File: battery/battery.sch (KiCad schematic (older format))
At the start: 40 parts, among them J1 batt_1, J2 batt_2, J3 batt_3, J4 batt_4, J5 reed_switch, J6 toPcb+, J7 toPcb-, J8 on_signal, Q1 batt1_sw, Q2 batt2_sw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

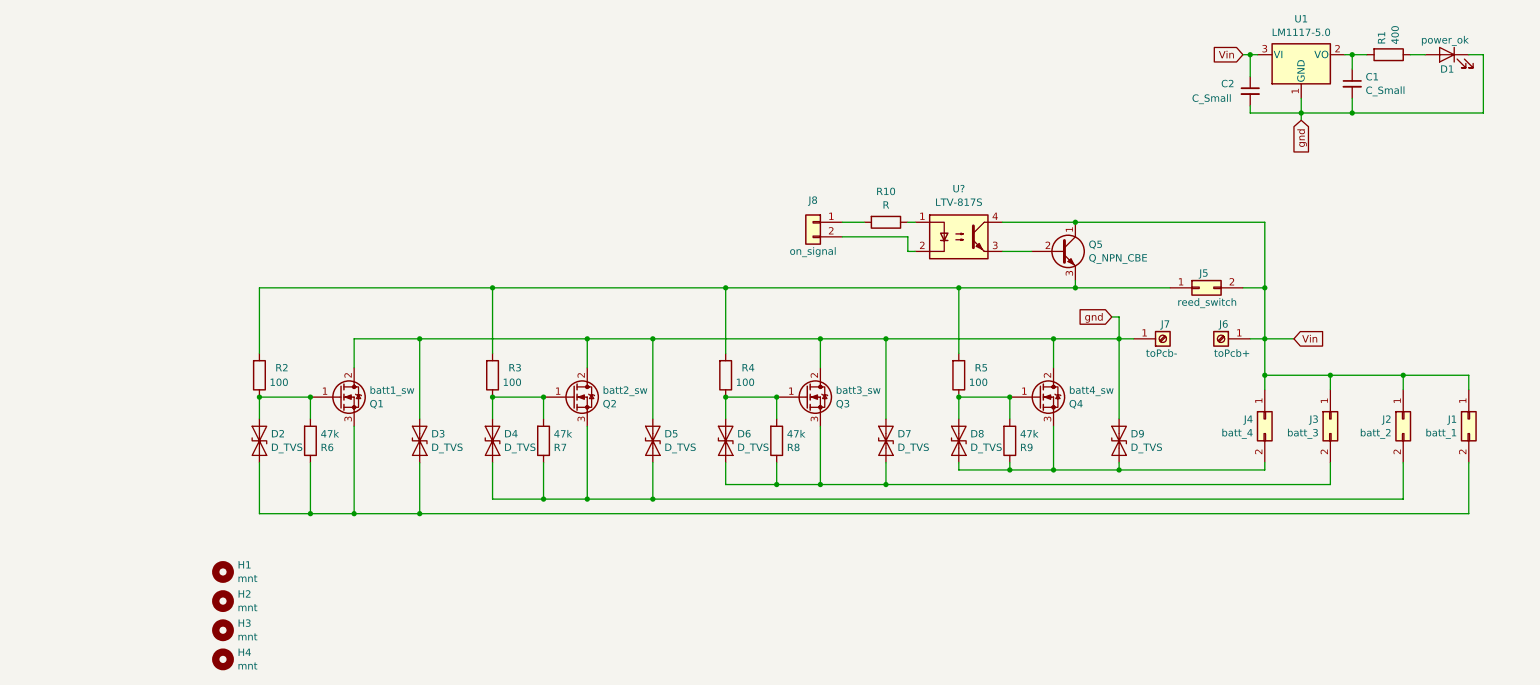
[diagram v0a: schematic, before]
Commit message: capacitor bybpas
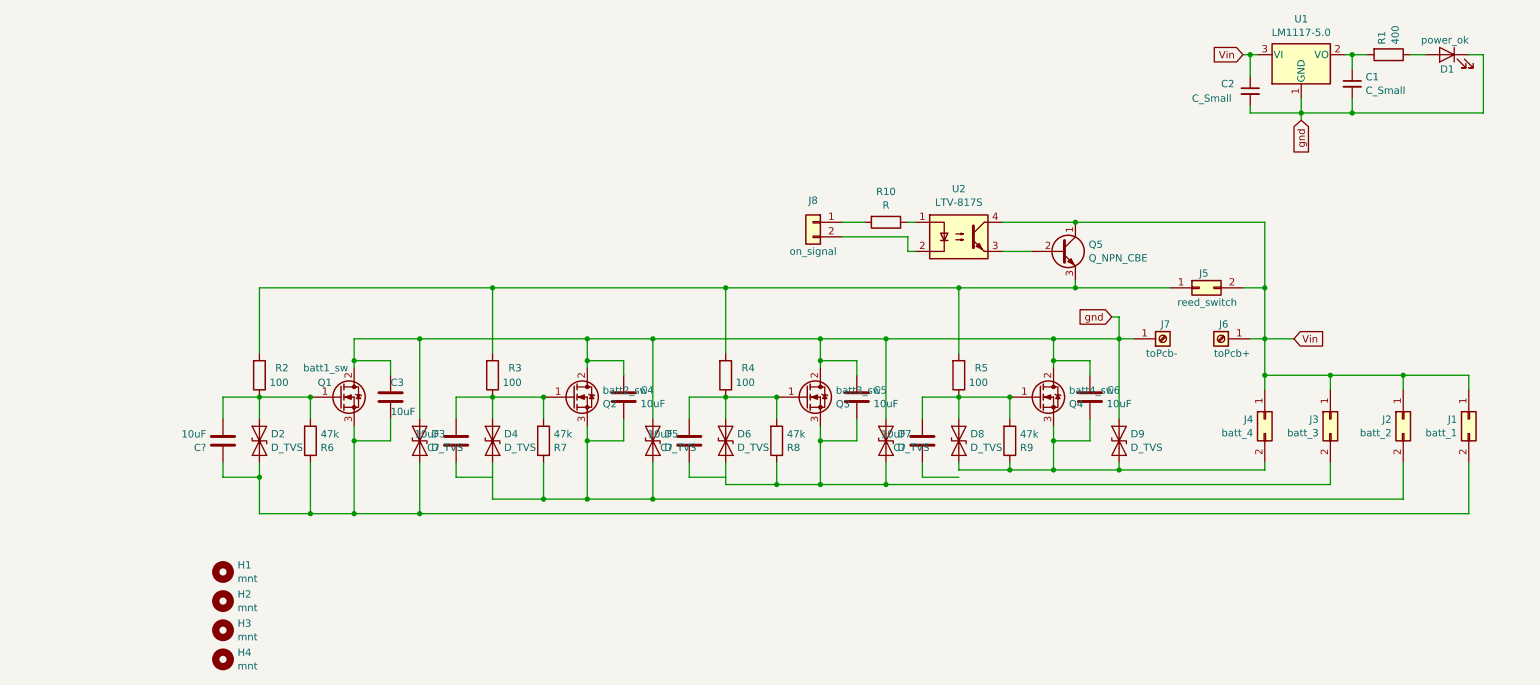
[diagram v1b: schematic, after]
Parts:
- added C3, C4, C5, C6, C? (x4): 10uF, Capacitor_SMD:C_0805_2012Metric_Pad1.15x1.40mm_HandSolder, symbol Device:C
- D2, D3, D4, D5, D6, D7, D8, D9: footprint Diode_SMD:D_SMB_Handsoldering -> Diode_SMD:D_SMB
- Q5: footprint Package_TO_SOT_THT:TO-92 -> Package_TO_SOT_SMD:SOT-23
- gave numbers to parts that had none: 1
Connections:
- net gnd: now also C3.1, C4.1, C5.1, C6.1
- net at D2.1 (A1), Q1.1 (G), R2.1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: now also C?.2
- net at D2.2 (A2), D3.2 (A2), J1.2 (Pin_2)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: now also C3.2, C?.1
- net at D4.2 (A2), D5.2 (A2), J2.2 (Pin_2)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: now also C4.2
- net at D6.2 (A2), D7.2 (A2), J3.2 (Pin_2)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: now also C5.2
- net at D8.2 (A2), D9.2 (A2), J4.2 (Pin_2)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: now also C6.2
- net at D4.1 (A1), Q2.1 (G), R3.1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: now also C?.2
- net at D6.1 (A1), Q3.1 (G), R4.1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: now also C?.2
- net at D8.1 (A1), Q4.1 (G), R5.1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: now also C?.2
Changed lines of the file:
@@
 U 1 1 5CF2C58F
 P 3000 3150
-F 0 "Q1" H 3206 3103 50  0000 L CNN
-F 1 "batt1_sw" H 3206 3196 50  0000 L CNN
+F 0 "Q1" H 2850 3250 50  0000 L CNN
+F 1 "batt1_sw" H 2750 3350 50  0000 L CNN
 F 2 "Package_TO_SOT_SMD:TO-252-2" H 3200 3250 50  0001 C CNN
 F 3 "~" H 3000 3150 50  0001 C CNN
@@
 F 0 "D3" V 3503 3529 50  0000 L CNN
 F 1 "D_TVS" V 3596 3529 50  0000 L CNN
-F 2 "Diode_SMD:D_SMB_Handsoldering" H 3550 3450 50  0001 C CNN
+F 2 "Diode_SMD:D_SMB" H 3550 3450 50  0001 C CNN
 F 3 "~" H 3550 3450 50  0001 C CNN
 	1    3550 3450
@@
 F 0 "D2" V 2403 3529 50  0000 L CNN
 F 1 "D_TVS" V 2496 3529 50  0000 L CNN
-F 2 "Diode_SMD:D_SMB_Handsoldering" H 2450 3450 50  0001 C CNN
+F 2 "Diode_SMD:D_SMB" H 2450 3450 50  0001 C CNN
 F 3 "~" H 2450 3450 50  0001 C CNN
 	1    2450 3450
@@
 F 0 "D5" V 5103 3529 50  0000 L CNN
 F 1 "D_TVS" V 5196 3529 50  0000 L CNN
-F 2 "Diode_SMD:D_SMB_Handsoldering" H 5150 3450 50  0001 C CNN
+F 2 "Diode_SMD:D_SMB" H 5150 3450 50  0001 C CNN
 F 3 "~" H 5150 3450 50  0001 C CNN
 	1    5150 3450
@@
 F 0 "D4" V 4003 3529 50  0000 L CNN
 F 1 "D_TVS" V 4096 3529 50  0000 L CNN
-F 2 "Diode_SMD:D_SMB_Handsoldering" H 4050 3450 50  0001 C CNN
+F 2 "Diode_SMD:D_SMB" H 4050 3450 50  0001 C CNN
 F 3 "~" H 4050 3450 50  0001 C CNN
 	1    4050 3450
@@
 F 0 "D7" V 6703 3529 50  0000 L CNN
 F 1 "D_TVS" V 6796 3529 50  0000 L CNN
-F 2 "Diode_SMD:D_SMB_Handsoldering" H 6750 3450 50  0001 C CNN
+F 2 "Diode_SMD:D_SMB" H 6750 3450 50  0001 C CNN
 F 3 "~" H 6750 3450 50  0001 C CNN
 	1    6750 3450
@@
 F 0 "D6" V 5603 3529 50  0000 L CNN
 F 1 "D_TVS" V 5696 3529 50  0000 L CNN
-F 2 "Diode_SMD:D_SMB_Handsoldering" H 5650 3450 50  0001 C CNN
+F 2 "Diode_SMD:D_SMB" H 5650 3450 50  0001 C CNN
 F 3 "~" H 5650 3450 50  0001 C CNN
 	1    5650 3450
@@
 Wire Wire Line
 	6300 3750 6750 3750
-Wire Wire Line
-	7900 3350 7900 3650
 Connection ~ 7900 3650
 Wire Wire Line
@@
 F 0 "D9" V 8303 3529 50  0000 L CNN
 F 1 "D_TVS" V 8396 3529 50  0000 L CNN
-F 2 "Diode_SMD:D_SMB_Handsoldering" H 8350 3450 50  0001 C CNN
+F 2 "Diode_SMD:D_SMB" H 8350 3450 50  0001 C CNN
 F 3 "~" H 8350 3450 50  0001 C CNN
 	1    8350 3450
@@
 F 0 "D8" V 7203 3529 50  0000 L CNN
 F 1 "D_TVS" V 7296 3529 50  0000 L CNN
-F 2 "Diode_SMD:D_SMB_Handsoldering" H 7250 3450 50  0001 C CNN
+F 2 "Diode_SMD:D_SMB" H 7250 3450 50  0001 C CNN
 F 3 "~" H 7250 3450 50  0001 C CNN
 	1    7250 3450
@@
 Connection ~ 7250 3150
 Wire Wire Line
-	3100 2750 3100 2950
+	3100 2750 3100 2900
 Wire Wire Line
 	3550 2750 3550 3300
 Connection ~ 3550 2750
-Wire Wire Line
-	3550 2750 3100 2750
-Wire Wire Line
-	4700 2750 4700 2950
 Connection ~ 4700 2750
 Wire Wire Line
@@
 Wire Wire Line
 	5150 2750 4700 2750
-Wire Wire Line
-	6300 2750 6300 2950
 Connection ~ 6300 2750
 Wire Wire Line
@@
 Wire Wire Line
 	6750 2750 6300 2750
-Wire Wire Line
-	7900 2750 7900 2950
 Connection ~ 7900 2750
 Wire Wire Line
@@
 	2450 3950 2800 3950
 Wire Wire Line
-	2450 3600 2450 3950
+	2450 3600 2450 3700
 Wire Wire Line
 	2800 3600 2800 3950
@@
 	2800 3950 3100 3950
 Wire Wire Line
-	3100 3350 3100 3950
+	3100 3350 3100 3450
 Wire Wire Line
 	3550 3600 3550 3950
@@
 	4400 3600 4400 3850
 Wire Wire Line
-	4700 3350 4700 3850
-Wire Wire Line
 	5150 3600 5150 3850
 Wire Wire Line
@@
 Wire Wire Line
 	6000 3600 6000 3750
-Wire Wire Line
-	6300 3350 6300 3750
 Wire Wire Line
 	6750 3600 6750 3750
@@
 F 0 "Q5" H 8141 2197 50  0000 L CNN
 F 1 "Q_NPN_CBE" H 8141 2104 50  0000 L CNN
-F 2 "Package_TO_SOT_THT:TO-92" H 8150 2250 50  0001 C CNN
+F 2 "Package_TO_SOT_SMD:SOT-23" H 8150 2250 50  0001 C CNN
 F 3 "~" H 7950 2150 50  0001 C CNN
 	1    7950 2150
@@
 	8050 1950 9350 1950
 $Comp
-L Isolator:LTV-817S U?
+L Isolator:LTV-817S U2
 U 1 1 5D48BD4A
 P 7250 2050
-F 0 "U?" H 7250 2379 50  0000 C CNN
+F 0 "U2" H 7250 2379 50  0000 C CNN
 F 1 "LTV-817S" H 7250 2286 50  0000 C CNN
 F 2 "Package_DIP:SMDIP-4_W9.53mm" H 7250 1750 50  0001 C CNN
@@
 	1    0    0    -1
 $EndComp
+$Comp
+L Device:C C3
+U 1 1 5D1B82C7
+P 3350 3150
+F 0 "C3" H 3350 3250 50  0000 L CNN
+F 1 "10uF" H 3350 3050 50  0000 L CNN
+F 2 "Capacitor_SMD:C_0805_2012Metric_Pad1.15x1.40mm_HandSolder" H 3388 3000 50  0001 C CNN
+F 3 "~" H 3350 3150 50  0001 C CNN
+	1    3350 3150
+	1    0    0    -1
+$EndComp
+Wire Wire Line
+	3350 3300 3350 3450
+Wire Wire Line
+	3350 3450 3100 3450
+Connection ~ 3100 3450
+Wire Wire Line
+	3100 3450 3100 3950
+Wire Wire Line
+	3100 2750 3550 2750
+Wire Wire Line
+	3350 3000 3350 2900
+Wire Wire Line
+	3350 2900 3100 2900
+Connection ~ 3100 2900
+Wire Wire Line
+	3100 2900 3100 2950
+$Comp
+L Device:C C4
+U 1 1 5D1CD1AE
+P 4950 3150
+F 0 "C4" H 5065 3197 50  0000 L CNN
+F 1 "10uF" H 5065 3104 50  0000 L CNN
+F 2 "Capacitor_SMD:C_0805_2012Metric_Pad1.15x1.40mm_HandSolder" H 4988 3000 50  0001 C CNN
+F 3 "~" H 4950 3150 50  0001 C CNN
+	1    4950 3150
+	1    0    0    -1
+$EndComp
+Wire Wire Line
+	4950 3300 4950 3450
+Wire Wire Line
+	4950 3450 4700 3450
+Wire Wire Line
+	4950 3000 4950 2900
+Wire Wire Line
+	4950 2900 4700 2900
+$Comp
+L Device:C C5
+U 1 1 5D1D0F67
+P 6550 3150
+F 0 "C5" H 6665 3197 50  0000 L CNN
+F 1 "10uF" H 6665 3104 50  0000 L CNN
+F 2 "Capacitor_SMD:C_0805_2012Metric_Pad1.15x1.40mm_HandSolder" H 6588 3000 50  0001 C CNN
+F 3 "~" H 6550 3150 50  0001 C CNN
+	1    6550 3150
+	1    0    0    -1
+$EndComp
+Wire Wire Line
+	6550 3300 6550 3450
+Wire Wire Line
+	6550 3450 6300 3450
+Wire Wire Line
+	6550 3000 6550 2900
+Wire Wire Line
+	6550 2900 6300 2900
+$Comp
+L Device:C C6
+U 1 1 5D1D97C7
+P 8150 3150
+F 0 "C6" H 8265 3197 50  0000 L CNN
+F 1 "10uF" H 8265 3104 50  0000 L CNN
+F 2 "Capacitor_SMD:C_0805_2012Metric_Pad1.15x1.40mm_HandSolder" H 8188 3000 50  0001 C CNN
+F 3 "~" H 8150 3150 50  0001 C CNN
+	1    8150 3150
+	1    0    0    -1
+$EndComp
+Wire Wire Line
+	8150 3300 8150 3450
+Wire Wire Line
+	8150 3450 7900 3450
+Wire Wire Line
+	8150 3000 8150 2900
+Wire Wire Line
+	8150 2900 7900 2900
+Wire Wire Line
+	4700 2750 4700 2900
+Connection ~ 4700 2900
+Wire Wire Line
+	4700 2900 4700 2950
+Wire Wire Line
+	4700 3350 4700 3450
+Connection ~ 4700 3450
+Wire Wire Line
+	4700 3450 4700 3850
+Wire Wire Line
+	6300 3350 6300 3450
+Connection ~ 6300 3450
+Wire Wire Line
+	6300 3450 6300 3750
+Wire Wire Line
+	6300 2750 6300 2900
+Connection ~ 6300 2900
+Wire Wire Line
+	6300 2900 6300 2950
+Wire Wire Line
+	7900 2750 7900 2900
+Connection ~ 7900 2900
+Wire Wire Line
+	7900 2900 7900 2950
+Wire Wire Line
+	7900 3350 7900 3450
+Connection ~ 7900 3450
+Wire Wire Line
+	7900 3450 7900 3650
+$Comp
+L Device:C C?
+U 1 1 5D206E7C
+P 2200 3450
+F 0 "C?" H 2315 3497 50  0000 L CNN
+F 1 "10uF" H 2315 3404 50  0000 L CNN
+F 2 "Capacitor_SMD:C_0805_2012Metric_Pad1.15x1.40mm_HandSolder" H 2238 3300 50  0001 C CNN
+F 3 "~" H 2200 3450 50  0001 C CNN
+	1    2200 3450
+	-1   0    0    1
+$EndComp
+Wire Wire Line
+	2200 3300 2200 3150
+Wire Wire Line
+	2200 3150 2450 3150
+Wire Wire Line
+	2200 3600 2200 3700
+Wire Wire Line
+	2200 3700 2450 3700
+Connection ~ 2450 3700
+Wire Wire Line
+	2450 3700 2450 3950
+$Comp
+L Device:C C?
+U 1 1 5D21C25D
+P 3800 3450
+F 0 "C?" H 3915 3497 50  0000 L CNN
+F 1 "10uF" H 3915 3404 50  0000 L CNN
+F 2 "Capacitor_SMD:C_0805_2012Metric_Pad1.15x1.40mm_HandSolder" H 3838 3300 50  0001 C CNN
+F 3 "~" H 3800 3450 50  0001 C CNN
+	1    3800 3450
+	-1   0    0    1
+$EndComp
+Wire Wire Line
+	3800 3300 3800 3150
+Wire Wire Line
+	3800 3150 4050 3150
+Wire Wire Line
+	3800 3600 3800 3700
+Wire Wire Line
+	3800 3700 4050 3700
+$Comp
+L Device:C C?
+U 1 1 5D221EA2
+P 5400 3450
+F 0 "C?" H 5515 3497 50  0000 L CNN
+F 1 "10uF" H 5515 3404 50  0000 L CNN
+F 2 "Capacitor_SMD:C_0805_2012Metric_Pad1.15x1.40mm_HandSolder" H 5438 3300 50  0001 C CNN
+F 3 "~" H 5400 3450 50  0001 C CNN
+	1    5400 3450
+	-1   0    0    1
+$EndComp
+Wire Wire Line
+	5400 3300 5400 3150
+Wire Wire Line
+	5400 3150 5650 3150
+Wire Wire Line
+	5400 3600 5400 3700
+Wire Wire Line
+	5400 3700 5650 3700
+$Comp
+L Device:C C?
+U 1 1 5D22807A
+P 7000 3450
+F 0 "C?" H 7115 3497 50  0000 L CNN
+F 1 "10uF" H 7115 3404 50  0000 L CNN
+F 2 "Capacitor_SMD:C_0805_2012Metric_Pad1.15x1.40mm_HandSolder" H 7038 3300 50  0001 C CNN
+F 3 "~" H 7000 3450 50  0001 C CNN
+	1    7000 3450
+	-1   0    0    1
+$EndComp
+Wire Wire Line
+	7000 3300 7000 3150
+Wire Wire Line
+	7000 3150 7250 3150
+Wire Wire Line
+	7000 3600 7000 3700
+Wire Wire Line
+	7000 3700 7250 3700
 $EndSCHEMATC

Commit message: fix
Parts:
- removed C? (x4): 10uF, Capacitor_SMD:C_0805_2012Metric_Pad1.15x1.40mm_HandSolder, symbol Device:C
- added C10, C7, C8, C9: 100n, Capacitor_SMD:C_0805_2012Metric_Pad1.15x1.40mm_HandSolder, symbol Device:C
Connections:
- net at D2.1 (A1), Q1.1 (G), R2.1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: now also C7.2
- net at C3.2, D2.2 (A2), D3.2 (A2)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: now also C7.1
- net at C4.2, D4.2 (A2), D5.2 (A2)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: now also C8.1
- net at C5.2, D6.2 (A2), D7.2 (A2)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: now also C9.1
- net at C6.2, D8.2 (A2), D9.2 (A2)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: now also C10.1
- net at D4.1 (A1), Q2.1 (G), R3.1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: now also C8.2
- net at D6.1 (A1), Q3.1 (G), R4.1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: now also C9.2
- net at D8.1 (A1), Q4.1 (G), R5.1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: now also C10.2
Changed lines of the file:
@@
 	2450 3950 2800 3950
-Wire Wire Line
-	2450 3600 2450 3700
 Wire Wire Line
 	2800 3600 2800 3950
@@
 	3550 3600 3550 3950
 Wire Wire Line
-	4050 3600 4050 3850
-Wire Wire Line
 	4400 3600 4400 3850
 Wire Wire Line
 	5150 3600 5150 3850
-Wire Wire Line
-	5650 3600 5650 3750
 Wire Wire Line
 	6000 3600 6000 3750
@@
 Wire Wire Line
 	7250 2850 7250 2400
-Connection ~ 7250 2400
-Wire Wire Line
-	7250 2400 8050 2400
 Wire Wire Line
 	5650 2850 5650 2400
@@
 Wire Wire Line
 	8050 2350 8050 2400
-Connection ~ 8050 2400
 Wire Wire Line
 	8050 2400 8700 2400
@@
 Wire Wire Line
 	7900 3450 7900 3650
-$Comp
-L Device:C C?
-U 1 1 5D206E7C
+Wire Wire Line
+	7250 2400 8050 2400
+Connection ~ 7250 2400
+Connection ~ 8050 2400
+$Comp
+L Device:C C7
+U 1 1 5D247DA5
 P 2200 3450
-F 0 "C?" H 2315 3497 50  0000 L CNN
-F 1 "10uF" H 2315 3404 50  0000 L CNN
+F 0 "C7" H 2085 3403 50  0000 R CNN
+F 1 "100n" H 2085 3496 50  0000 R CNN
 F 2 "Capacitor_SMD:C_0805_2012Metric_Pad1.15x1.40mm_HandSolder" H 2238 3300 50  0001 C CNN
 F 3 "~" H 2200 3450 50  0001 C CNN
@@
 Wire Wire Line
 	2200 3700 2450 3700
-Connection ~ 2450 3700
-Wire Wire Line
-	2450 3700 2450 3950
-$Comp
-L Device:C C?
-U 1 1 5D21C25D
+$Comp
+L Device:C C8
+U 1 1 5D24D386
 P 3800 3450
-F 0 "C?" H 3915 3497 50  0000 L CNN
-F 1 "10uF" H 3915 3404 50  0000 L CNN
+F 0 "C8" H 3685 3403 50  0000 R CNN
+F 1 "100n" H 3685 3496 50  0000 R CNN
 F 2 "Capacitor_SMD:C_0805_2012Metric_Pad1.15x1.40mm_HandSolder" H 3838 3300 50  0001 C CNN
 F 3 "~" H 3800 3450 50  0001 C CNN
@@
 	3800 3700 4050 3700
 $Comp
-L Device:C C?
-U 1 1 5D221EA2
+L Device:C C9
+U 1 1 5D252E37
 P 5400 3450
-F 0 "C?" H 5515 3497 50  0000 L CNN
-F 1 "10uF" H 5515 3404 50  0000 L CNN
+F 0 "C9" H 5285 3403 50  0000 R CNN
+F 1 "100n" H 5285 3496 50  0000 R CNN
 F 2 "Capacitor_SMD:C_0805_2012Metric_Pad1.15x1.40mm_HandSolder" H 5438 3300 50  0001 C CNN
 F 3 "~" H 5400 3450 50  0001 C CNN
@@
 	5400 3700 5650 3700
 $Comp
-L Device:C C?
-U 1 1 5D22807A
+L Device:C C10
+U 1 1 5D258E5B
 P 7000 3450
-F 0 "C?" H 7115 3497 50  0000 L CNN
-F 1 "10uF" H 7115 3404 50  0000 L CNN
+F 0 "C10" H 6885 3403 50  0000 R CNN
+F 1 "100n" H 6885 3496 50  0000 R CNN
 F 2 "Capacitor_SMD:C_0805_2012Metric_Pad1.15x1.40mm_HandSolder" H 7038 3300 50  0001 C CNN
 F 3 "~" H 7000 3450 50  0001 C CNN
@@
 Wire Wire Line
 	7000 3700 7250 3700
+Wire Wire Line
+	2450 3600 2450 3700
+Connection ~ 2450 3700
+Wire Wire Line
+	2450 3700 2450 3950
+Wire Wire Line
+	4050 3600 4050 3700
+Connection ~ 4050 3700
+Wire Wire Line
+	4050 3700 4050 3850
+Wire Wire Line
+	5650 3600 5650 3700
+Connection ~ 5650 3700
+Wire Wire Line
+	5650 3700 5650 3750
+Wire Wire Line
+	7250 3700 7250 3650
+Connection ~ 7250 3650
 $EndSCHEMATC

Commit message: new schematic
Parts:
- removed Q5: Q_NPN_CBE, Package_TO_SOT_SMD:SOT-23, symbol Device:Q_NPN_CBE
- added D10, D11, D12, D13: bat48, Diode_THT:D_DO-35_SOD27_P10.16mm_Horizontal, symbol Device:D_Schottky
- added Q5: BC817-25, Package_TO_SOT_SMD:SOT-23_Handsoldering, symbol Device:Q_NPN_BEC
- added R11: 10k, Resistor_SMD:R_0805_2012Metric, symbol Device:R
- C3, C4, C5, C6: footprint Capacitor_SMD:C_0805_2012Metric_Pad1.15x1.40mm_HandSolder -> Capacitor_SMD:C_1206_3216Metric_Pad1.42x1.75mm_HandSolder
- Q1, Q2, Q3, Q4: footprint Package_TO_SOT_SMD:TO-252-2 -> Package_TO_SOT_SMD:TO-263-2
- R10: value R -> 680
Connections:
- net Vin: now also Q5.3 (C)
- net at U2.3: now also Q5.1 (B), R11.2
- new net: D10.2 (A), D11.2 (A), D12.2 (A), D13.2 (A), J5.1 (Pin_1), Q5.2 (E), R11.1
- new net: D11.1 (K), R3.2
- new net: D12.1 (K), R4.2
- new net: D13.1 (K), R5.2
- new net: D10.1 (K), R2.2
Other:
- moved on the sheet: J8, R10, U2

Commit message: visual fix
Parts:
- C1, C2: value C_Small -> 100n
- D10: value bat48 -> BAT48
- D2, D3, D4, D5, D6, D7, D8, D9: value D_TVS -> P6SMB18CA
- Q1: value batt1_sw -> IRL2203N
- Q2: value batt2_sw -> IRL2203N
- Q3: value batt3_sw -> IRL2203N
- Q4: value batt4_sw -> IRL2203N
- R2: value 100 -> 680
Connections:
- net gnd: no longer C6.1, D9.1 (A1), Q4.2 (D)
- new net: C6.1, D9.1 (A1), Q4.2 (D)
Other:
- moved on the sheet: C1, C10, C2, C3, C4, C5, C6, C7, C8, C9, D1, D10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

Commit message: Some work
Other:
- note added: "Sygnalizacja stanu układu\nLed1 On - power on\nLed1 Off - power off"
- note added: "Włącznik na kontaktronie"
- note added: "włącznik na transoptorze\nsterowanie sygnałem z częsci logicznej"
- moved on the sheet: C1, C10, C2, C3, C4, C5, C6, C7, C8, C9, D1, D10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
